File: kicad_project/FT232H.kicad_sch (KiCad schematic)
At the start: 25 parts, among them U10 FT232H, U11 SN74CB3Q3253PWR, U12 SN74CB3Q3253PWR

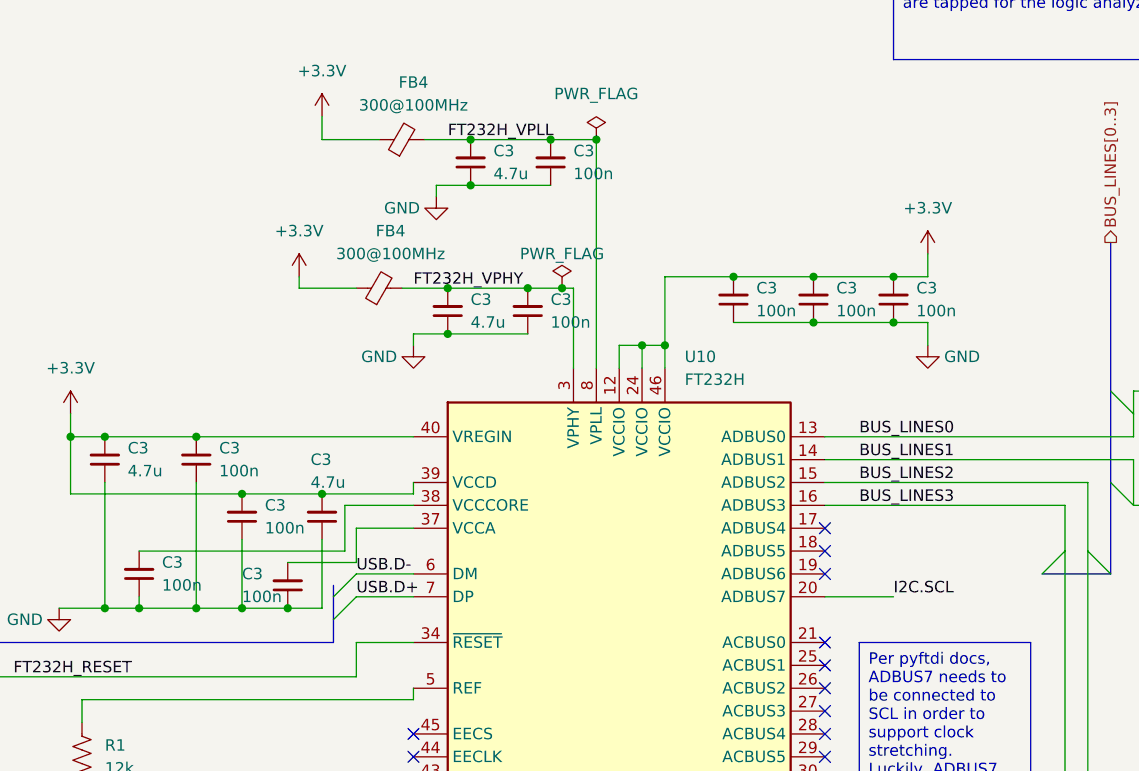
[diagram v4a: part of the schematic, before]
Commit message: Add part numbers for capacitors, start working on BoM job
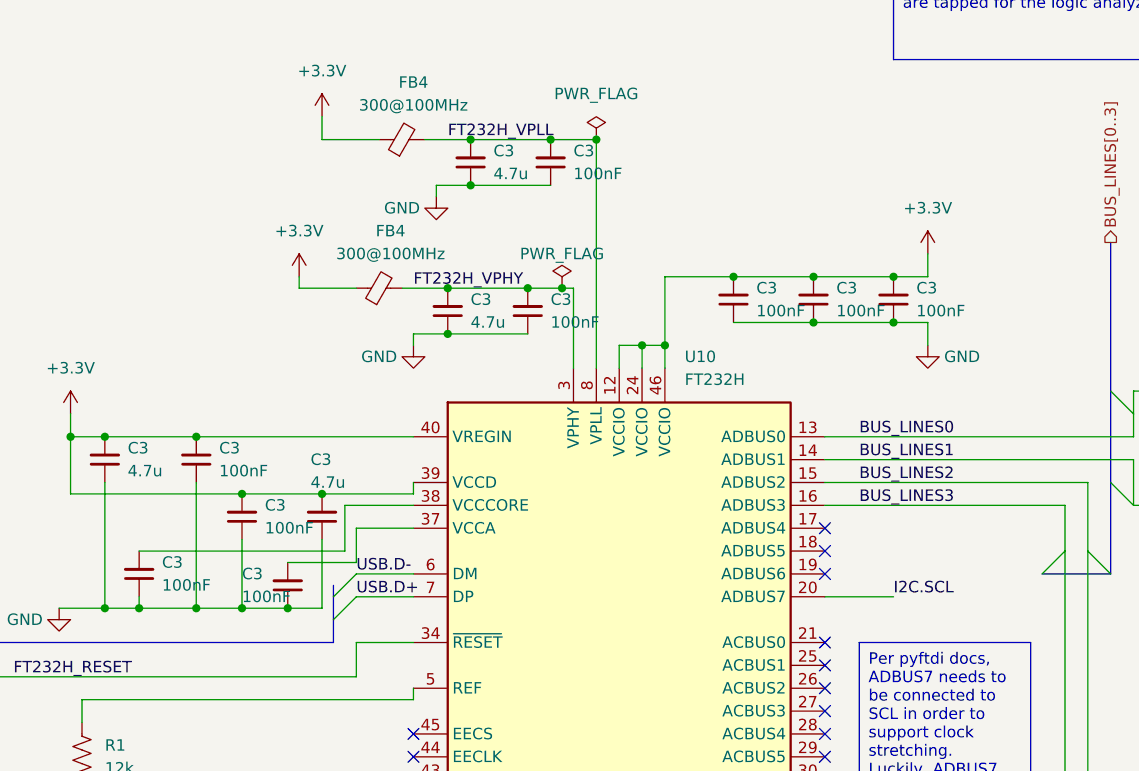
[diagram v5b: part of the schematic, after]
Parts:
- C3: LibRef (none) -> CL31B475KBHNNNE; Supplier (none) -> Digi-Key
- C3: value 100n -> 100nF; LibRef (none) -> GRM319R72A104KA01D; Supplier (none) -> Digi-Key
- C3: LibRef (none) -> C1206C103J5RACTU; Supplier (none) -> Digi-Key
- FB4, R1, U10, U11, U12: Supplier (none) -> Digi-Key

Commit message: Fill in all part numbers, add pcbinv bom job
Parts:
- FB4: LibRef (none) -> 742792121
- R1: LibRef (none) -> ERJ-8ENF1002V; SKU (none) -> P10.0KFCT-ND
- R1: LibRef (none) -> ERJ-8ENF1202V; SKU (none) -> P12.0KFCT-ND
- U11, U12: SKU (none) -> 296-19135-1-ND
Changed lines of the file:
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@@
+      (effects (font (size 1.27 1.27)) hide)
+    )
+    (property "SKU" "296-19135-1-ND" (at 242.57 93.98 0)
       (effects (font (size 1.27 1.27)) hide)
     )
@@
       (effects (font (size 1.27 1.27)) hide)
     )
-    (property "LibRef" "" (at 102.87 60.96 0)
+    (property "LibRef" "742792121" (at 102.87 60.96 0)
+      (effects (font (size 1.27 1.27)) hide)
+    )
+    (property "Description" "FERRITE BEAD 300 OHM 1206 1LN" (at 102.87 60.96 0)
       (effects (font (size 1.27 1.27)) hide)
     )
@@
       (effects (font (size 1.27 1.27)) hide)
     )
-    (property "LibRef" "" (at 297.18 139.7 0)
+    (property "LibRef" "ERJ-8ENF1002V" (at 297.18 139.7 0)
+      (effects (font (size 1.27 1.27)) hide)
+    )
+    (property "SKU" "P10.0KFCT-ND" (at 297.18 139.7 0)
       (effects (font (size 1.27 1.27)) hide)
     )
@@
       (effects (font (size 1.27 1.27)) hide)
     )
-    (property "LibRef" "" (at 100.33 77.47 0)
+    (property "LibRef" "742792121" (at 100.33 77.47 0)
+      (effects (font (size 1.27 1.27)) hide)
+    )
+    (property "Description" "FERRITE BEAD 300 OHM 1206 1LN" (at 100.33 77.47 0)
       (effects (font (size 1.27 1.27)) hide)
     )
@@
       (effects (font (size 1.27 1.27)) hide)
     )
-    (property "LibRef" "" (at 49.53 127 0)
+    (property "LibRef" "ERJ-8ENF1002V" (at 49.53 127 0)
+      (effects (font (size 1.27 1.27)) hide)
+    )
+    (property "SKU" "P10.0KFCT-ND" (at 49.53 127 0)
       (effects (font (size 1.27 1.27)) hide)
     )
@@
       (effects (font (size 1.27 1.27)) hide)
     )
-    (property "LibRef" "" (at 304.8 205.74 0)
+    (property "LibRef" "ERJ-8ENF1002V" (at 304.8 205.74 0)
+      (effects (font (size 1.27 1.27)) hide)
+    )
+    (property "SKU" "P10.0KFCT-ND" (at 304.8 205.74 0)
       (effects (font (size 1.27 1.27)) hide)
     )
@@
       (effects (font (size 1.27 1.27)) hide)
     )
-    (property "LibRef" "" (at 67.31 129.54 0)
+    (property "LibRef" "ERJ-8ENF1202V" (at 67.31 129.54 0)
+      (effects (font (size 1.27 1.27)) hide)
+    )
+    (property "Description" "RES SMD 12k Ohm 1% 1/4W 1206" (at 67.31 129.54 0)
+      (effects (font (size 1.27 1.27)) hide)
+    )
+    (property "SKU" "P12.0KFCT-ND" (at 67.31 129.54 0)
       (effects (font (size 1.27 1.27)) hide)
     )
@@
       (effects (font (size 1.27 1.27)) hide)
     )
-    (property "LibRef" "" (at 299.72 205.74 0)
+    (property "LibRef" "ERJ-8ENF1002V" (at 299.72 205.74 0)
+      (effects (font (size 1.27 1.27)) hide)
+    )
+    (property "SKU" "P10.0KFCT-ND" (at 299.72 205.74 0)
       (effects (font (size 1.27 1.27)) hide)
     )
@@
       (effects (font (size 1.27 1.27)) hide)
     )
-    (property "LibRef" "" (at 77.47 135.89 0)
+    (property "LibRef" "ERJ-8ENF1002V" (at 77.47 135.89 0)
+      (effects (font (size 1.27 1.27)) hide)
+    )
+    (property "SKU" "P10.0KFCT-ND" (at 77.47 135.89 0)
       (effects (font (size 1.27 1.27)) hide)
     )
@@
       (effects (font (size 1.27 1.27)) hide)
     )
+    (property "SKU" "296-19135-1-ND" (at 242.57 144.78 0)
+      (effects (font (size 1.27 1.27)) hide)
+    )

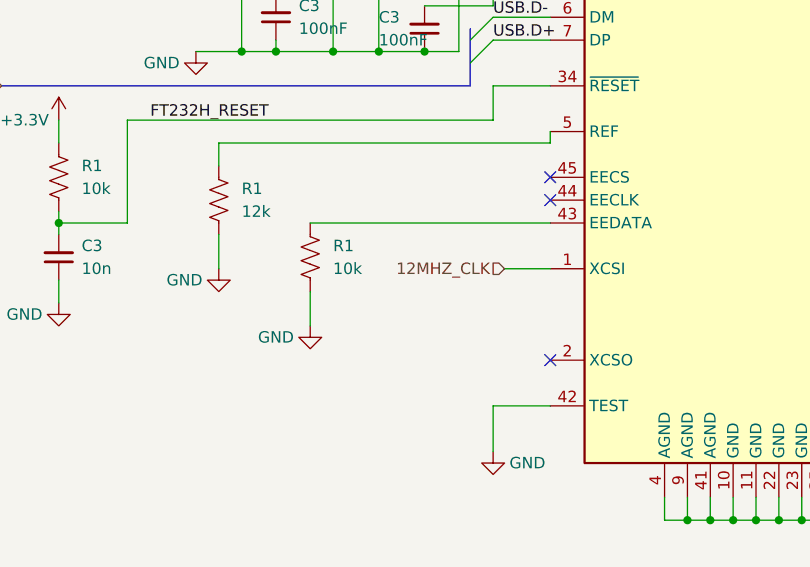
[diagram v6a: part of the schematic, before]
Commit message: Add diode on SD card CS line, fix position of PWM/analog testing capacitor
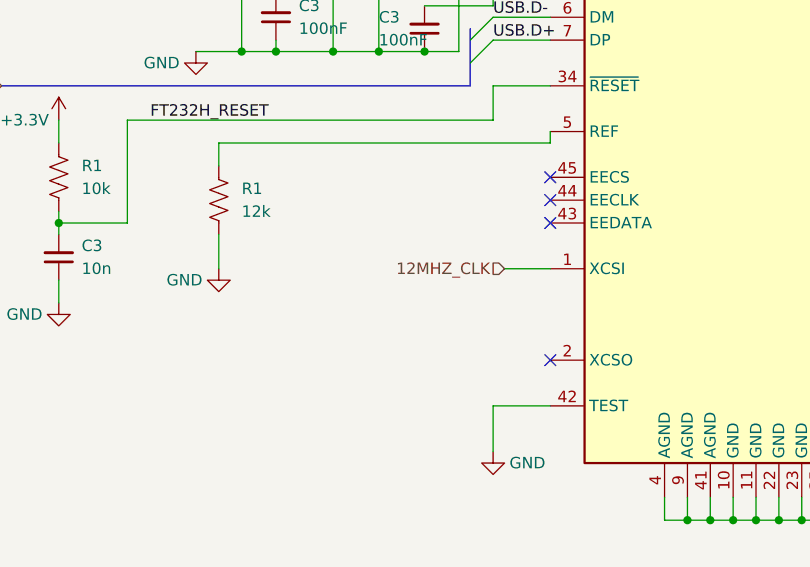
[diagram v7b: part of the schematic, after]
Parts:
- removed R1: 10k, Resistor_SMD:R_1206_3216Metric, symbol Device:R_US
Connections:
- no-connect marks 22 -> 23
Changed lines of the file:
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@@
   (no_connect (at 149.86 127))
   (no_connect (at 149.86 104.14))
+  (no_connect (at 104.14 132.08))
   (no_connect (at 149.86 109.22))
   (no_connect (at 149.86 121.92))
@@
     (stroke (width 0) (type default))
   )
-  (wire (pts (xy 77.47 139.7) (xy 77.47 143.51))
-    (stroke (width 0) (type default))
-  )
   (wire (pts (xy 256.54 142.24) (xy 270.51 142.24))
     (stroke (width 0) (type default))
@@
   )
   (wire (pts (xy 121.92 162.56) (xy 121.92 165.1))
-    (stroke (width 0) (type default))
-  )
-  (wire (pts (xy 77.47 132.08) (xy 104.14 132.08))
     (stroke (width 0) (type default))
   )
@@
         (path "/a0f40274-9469-4bcf-885c-e8b8a490ea54/a2280405-5315-4fe3-be7c-fd34d4bf90fe"
           (reference "R23") (unit 1)
-        )
-      )
-    )
-  )
-  (symbol (lib_id "Device:R_US") (at 77.47 135.89 0) (unit 1)
-    (in_bom yes) (on_board yes) (dnp no) (fields_autoplaced)
-    (property "Reference" "R1" (at 80.01 134.62 0)
-      (effects (font (size 1.27 1.27)) (justify left))
-    )
-    (property "Value" "10k" (at 80.01 137.16 0)
-      (effects (font (size 1.27 1.27)) (justify left))
-    )
-    (property "Footprint" "Resistor_SMD:R_1206_3216Metric" (at 78.486 136.144 90)
-      (effects (font (size 1.27 1.27)) hide)
-    )
-    (property "Datasheet" "~" (at 77.47 135.89 0)
-      (effects (font (size 1.27 1.27)) hide)
-    )
-    (property "Supplier" "Digi-Key" (at 77.47 135.89 0)
-      (effects (font (size 1.27 1.27)) hide)
-    )
-    (property "LibRef" "ERJ-8ENF1002V" (at 77.47 135.89 0)
-      (effects (font (size 1.27 1.27)) hide)
-    )
-    (property "SKU" "P10.0KFCT-ND" (at 77.47 135.89 0)
-      (effects (font (size 1.27 1.27)) hide)
-    )
-    (pin "1")
-    (pin "2")
-    (instances
-      (project "mbed-ce-ci-shield-v2"
-        (path "/a0f40274-9469-4bcf-885c-e8b8a490ea54"
-          (reference "R1") (unit 1)
-        )
-        (path "/a0f40274-9469-4bcf-885c-e8b8a490ea54/d2cb7c4f-a03f-4f1c-8cab-0427a0ad2909"
-          (reference "R13") (unit 1)
-        )
-        (path "/a0f40274-9469-4bcf-885c-e8b8a490ea54/a2280405-5315-4fe3-be7c-fd34d4bf90fe"
-          (reference "R29") (unit 1)
         )
       )
@@
         )
       )
-    )
-  )
-  (symbol (lib_id "power:GND") (at 77.47 143.51 0) (unit 1)
-    (in_bom yes) (on_board yes) (dnp no)
-    (property "Reference" "#PWR01" (at 77.47 149.86 0)
-      (effects (font (size 1.27 1.27)) hide)
-    )
-    (property "Value" "GND" (at 73.66 144.78 0)
-      (effects (font (size 1.27 1.27)))
-    )
-    (property "Footprint" "" (at 77.47 143.51 0)
-      (effects (font (size 1.27 1.27)) hide)
-    )
-    (property "Datasheet" "" (at 77.47 143.51 0)
-      (effects (font (size 1.27 1.27)) hide)
-    )
-    (pin "1")
-    (instances
-      (project "mbed-ce-ci-shield-v2"
-        (path "/a0f40274-9469-4bcf-885c-e8b8a490ea54"
-          (reference "#PWR01") (unit 1)
-        )
-        (path "/a0f40274-9469-4bcf-885c-e8b8a490ea54/d2cb7c4f-a03f-4f1c-8cab-0427a0ad2909"
-          (reference "#PWR03") (unit 1)
-        )
-        (path "/a0f40274-9469-4bcf-885c-e8b8a490ea54/a2280405-5315-4fe3-be7c-fd34d4bf90fe"
-          (reference "#PWR062") (unit 1)
-        )
-      )
